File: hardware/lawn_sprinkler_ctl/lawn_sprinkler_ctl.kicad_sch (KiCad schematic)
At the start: 63 parts, among them J1 Terminal_01x14, J2 USB_C_Receptacle_USB2.0_16P, Q1 BT136-600, Q2 BT136-600, Q3 BT136-600, Q4 BT136-600, Q5 BT136-600, Q6 BT136-600, SW1 Reset, SW2 Cde_EV_1, SW3 Cd_EV_2, SW4 Cde_EV_3, SW5 Cde_EV_4, SW6 Cde_EV_5, SW7 Cde_EV_6, U1 mini_esp32, U2 MP1584EN, U3 MOC3041M, U4 MOC3041M, U5 MOC3041M, U6 MOC3041M, U7 MOC3041M, U8 MOC3041M

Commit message: kicad schematic V0.2
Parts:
- removed C2, C3, C4, C5, C6, C7, C8: 10nF, Capacitor_SMD:C_0805_2012Metric, symbol Device:C
- removed D+, Vbus: ~, Connector_JST:JST_PH_S4B-PH-K_1x04_P2.00mm_Horizontal, symbol Mechanical:MountingHole
- removed D-, GND: ~, symbol Mechanical:MountingHole
- removed J2: USB_C_Receptacle_USB2.0_16P, symbol Connector:USB_C_Receptacle_USB2.0_16P
- removed Q2, Q4, Q6: BT136-600, Package_TO_SOT_THT:TO-220F-3_Horizontal_TabDown, symbol Triac_Thyristor:BT136-600
- removed R20: 220, Resistor_SMD:R_0805_2012Metric, symbol Device:R
- added C2: 10uF, Capacitor_THT:CP_Radial_D8.0mm_P3.50mm, symbol Device:C_Polarized
- added D9: LED, symbol Device:LED
- added Q10, Q12: BT136-600, Package_TO_SOT_THT:TO-220-3_Vertical, symbol Triac_Thyristor:BT136-600
- added Q11, Q2, Q4, Q6, Q7, Q9: BC547, Package_TO_SOT_THT:TO-92_Inline, symbol Transistor_BJT:BC547
- added Q8: BT136-600, Package_TO_SOT_SMD:TO-252-3_TabPin2, symbol Triac_Thyristor:BT136-600
- added R21, R22, R24, R25, R26: 330, Resistor_SMD:R_0805_2012Metric, symbol Device:R
- added R23: 10k, symbol Device:R
- added R27: 330, symbol Device:R
- D1: value LED red -> LED
- D8: value LED blue -> LED
- Q1, Q3, Q5: footprint Package_TO_SOT_THT:TO-220F-3_Horizontal_TabDown -> Package_TO_SOT_THT:TO-220-3_Vertical
- R13, R17, R4, R5, R9: value 330 -> 10k; footprint Resistor_SMD:R_0805_2012Metric -> (none)
- U2: value MP1584EN -> FULARR_MP1584EN
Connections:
- net +3.3V: now also C2.1
- net 24VAC_2: now also R15.2, R7.2, Q10.2 (A2), Q12.2 (A2), Q8.2 (A2), R21.2, R25.2; no longer R14.2, R17.2, R5.2, R8.2
- net Cmd_1: now also R4.1; no longer U3.2
- net Cmd_2: now also R5.1; no longer U4.2
- net Cmd_3: now also R9.1; no longer U5.2
- net Cmd_4: now also R13.1; no longer U6.2
- net Cmd_5: now also R17.1; no longer U7.2
- net Cmd_6: now also R23.1; no longer U8.2
- net EV2: now also Q3.1 (A1), R8.2; no longer R6.2
- net EV3: now also Q5.1 (A1), R12.2; no longer Q3.1 (A1), R9.2
- net EV4: now also R16.2, Q8.1 (A1); no longer R12.2
- net EV5: now also Q10.1 (A1), R22.2; no longer Q5.1 (A1), R15.2
- net EV6: now also Q12.1 (A1), R26.2; no longer R18.2
- net GND: now also C2.2, D9.1 (K), Q11.3 (E), Q2.3 (E), Q4.3 (E), Q6.3 (E), Q7.3 (E), Q9.3 (E)
- net at R10.2: now also U5.1; no longer U6.1
- net at R12.1: now also Q5.3 (G), U5.4; no longer U6.4
- net at R11.1: now also U5.6; no longer U6.6
- net at D6.1 (K): now also R18.1; no longer R13.1
- net at U8.6: now also R25.1; no longer R17.1
- net at R8.1: now also Q3.3 (G), U4.4; no longer U5.6
- net at SW1.2: now also U1.2 (RST)
- net at R13.2: now also Q6.2 (B); no longer U7.1
- net at U7.6: now also R21.1; no longer R14.1
- net at D7.1 (K): now also R24.1; no longer R16.1
- net at U4.6: now also R7.1; no longer R5.1
- net at D3.1 (K): now also R6.1; no longer R4.1
- net at U4.1: now also R6.2; no longer R4.2
- net at D4.1 (K): now also R10.1; no longer R7.1
- net at U8.1: now also R24.2; no longer R16.2
- net at U8.4: now also Q12.3 (G), R26.1; no longer R18.1
- net at D5.1 (K): now also R14.1; no longer R10.1
- net at U1.27 (IO_21/D2/SDA): now also R27.1
- new net: D9.2 (A), R27.2
- new net: Q4.1 (C), U5.2
- new net: Q4.2 (B), R9.2
- new net: Q6.1 (C), U6.2
- new net: Q9.2 (B), R17.2
- new net: Q2.2 (B), R5.2
- new net: Q11.1 (C), U8.2
- new net: Q11.2 (B), R23.2
- new net: Q8.3 (G), R16.1, U6.4
- new net: Q7.1 (C), U3.2
- new net: Q7.2 (B), R4.2
- new net: Q2.1 (C), U4.2
- new net: R15.1, U6.6
- new net: R18.2, U7.1
- new net: Q9.1 (C), U7.2
- new net: Q10.3 (G), R22.1, U7.4
- new net: R14.2, U6.1
- no-connect marks 20 -> 26
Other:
- note added: "EVs command"
- note added: "EVs manual control"
- note added: "Microcontroller module"
- note added: "power supply"
- note added: "terminal to EVs, 24VAC"
- moved on the sheet: C1, D1, D2, Q1, R1, R19, R2, R3, SW1, U1, U3

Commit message: feat: update hardware
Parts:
- removed D7: LED, LED_THT:LED_D5.0mm, symbol Device:LED_Small
- removed D8, D9: LED, symbol Device:LED
- removed J1: Terminal_01x14, symbol Connector:Screw_Terminal_01x14
- removed Q11, Q9: BC547, Package_TO_SOT_THT:TO-92_Inline, symbol Transistor_BJT:BC547
- removed Q3, Q5: BT136-600, Package_TO_SOT_THT:TO-220-3_Vertical, symbol Triac_Thyristor:BT136-600
- removed R19: 330, symbol Device:R
- removed SW1: Reset, symbol Switch:SW_Push
- removed U1: mini_esp32, symbol ESP32_mini:mini_esp32
- removed U7, U8: MOC3041M, Package_DIP:DIP-6_W7.62mm, symbol Relay_SolidState:MOC3041M
- added D2, D8, D9: LED, LED_THT:LED_D5.0mm, symbol Device:LED_Small
- added J1, J10, J11, J12, J13, J14, J2, J3, J4, J5, J6, J7, J8, J9: Screw_Terminal_01x01, Carbonaro:square_pad, symbol Connector:Screw_Terminal_01x01
- added J15: Conn_01x04, Connector_PinHeader_2.54mm:PinHeader_1x06_P2.54mm_Vertical, symbol Connector_Generic:Conn_01x06
- added Q11, Q9: BT136-600, Package_TO_SOT_SMD:TO-252-3_TabPin2, symbol Triac_Thyristor:BT136-600
- added Q3, Q5: BC547, Package_TO_SOT_THT:TO-92_Inline, symbol Transistor_BJT:BC547
- added R2, R4: 10k, Resistor_SMD:R_0805_2012Metric_Pad1.20x1.40mm_HandSolder, symbol Device:R
- added R28, R29, R30, R31, R32: 330, Resistor_SMD:R_0805_2012Metric_Pad1.20x1.40mm_HandSolder, symbol Device:R
- added R33, R34: 1k, Resistor_SMD:R_0805_2012Metric_Pad1.20x1.40mm_HandSolder, symbol Device:R_Small
- added SW7: Reset, Button_Switch_THT:SW_PUSH-12mm_Wuerth-430476085716, symbol Switch:SW_Push
- added U2, U3: MOC3041M, Package_DIP:DIP-6_W7.62mm, symbol Relay_SolidState:MOC3041M
- added U8: ESP32-C6-DevKitC-1, Carbonaro:ESP32-C6_DevKit_N8, symbol Espressif:ESP32-C6-DevKitC-1
- C2: footprint Capacitor_THT:CP_Radial_D8.0mm_P3.50mm -> Capacitor_THT:C_Radial_D5.0mm_H11.0mm_P2.00mm
- Q10, Q12: footprint Package_TO_SOT_THT:TO-220-3_Vertical -> Package_TO_SOT_SMD:TO-252-3_TabPin2
- Q7: renamed from Q1; footprint Package_TO_SOT_THT:TO-220-3_Vertical -> Package_TO_SOT_SMD:TO-252-3_TabPin2
- R1: renamed from R4; footprint (none) -> Resistor_SMD:R_0805_2012Metric_Pad1.20x1.40mm_HandSolder
- R10, R11, R12, R21, R22, R24, R25, R26, R7, R8: footprint Resistor_SMD:R_0805_2012Metric -> Resistor_SMD:R_0805_2012Metric_Pad1.20x1.40mm_HandSolder
- R13, R17: value 10k -> 1k; footprint (none) -> Resistor_SMD:R_0805_2012Metric_Pad1.20x1.40mm_HandSolder
- R14, R15, R16, R18: value 330 -> 1k; footprint Resistor_SMD:R_0805_2012Metric -> Resistor_SMD:R_0805_2012Metric_Pad1.20x1.40mm_HandSolder
- R19: renamed from R1; footprint Resistor_SMD:R_0805_2012Metric -> Resistor_SMD:R_0805_2012Metric_Pad1.20x1.40mm_HandSolder
- R20: renamed from R2; footprint Resistor_SMD:R_0805_2012Metric -> Resistor_SMD:R_0805_2012Metric_Pad1.20x1.40mm_HandSolder
- R23, R9: value 10k -> 330; footprint (none) -> Resistor_SMD:R_0805_2012Metric_Pad1.20x1.40mm_HandSolder
- R27, R5: footprint (none) -> Resistor_SMD:R_0805_2012Metric_Pad1.20x1.40mm_HandSolder
- R3, R6: value 330 -> 10k; footprint Resistor_SMD:R_0805_2012Metric -> Resistor_SMD:R_0805_2012Metric_Pad1.20x1.40mm_HandSolder
- SW1: renamed from SW2; footprint (none) -> Button_Switch_THT:SW_PUSH-12mm_Wuerth-430476085716
- SW2: renamed from SW3; value Cd_EV_2 -> Cde_EV_2; footprint (none) -> Button_Switch_THT:SW_PUSH-12mm_Wuerth-430476085716
- SW3: renamed from SW4; footprint (none) -> Button_Switch_THT:SW_PUSH-12mm_Wuerth-430476085716
- SW4: renamed from SW5; footprint (none) -> Button_Switch_THT:SW_PUSH-12mm_Wuerth-430476085716
- SW5: renamed from SW6; footprint (none) -> Button_Switch_THT:SW_PUSH-12mm_Wuerth-430476085716
- SW6: renamed from SW7; footprint (none) -> Button_Switch_THT:SW_PUSH-12mm_Wuerth-430476085716
- U7: renamed from U2; footprint Olivier:FULARR_MP1584EN -> Carbonaro:FULARR_MP1584EN; symbol Olivier:FULARR_MP1584EN -> Carbonaro:FULARR_MP1584EN
- renumbered D2 to D7, Q7 to Q1, U3 to U1
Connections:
- net +3.3V: now also R10.1, R11.1, R12.1, R7.1, R8.1, R9.1, D2.2 (A), J15.1 (Pin_1), R33.1, R34.1, U8.1 (3V3)
- net 24VAC_1: now also J1.1 (Pin_1), J5.1 (Pin_1)
- net 24VAC_2: now also R23.2, R27.2, J2.1 (Pin_1), Q11.2 (A2), Q9.2 (A2), R29.2; no longer R11.2, R15.2, R7.2
- net Cmd_1: now also U8.23 (GPIO18)
- net Cmd_2: now also R2.1, U8.24 (GPIO19); no longer R5.1
- net Cmd_3: now also R3.1, U8.25 (GPIO20); no longer R9.1
- net Cmd_4: now also R4.1, U8.26 (GPIO21); no longer R13.1
- net Cmd_5: now also R5.1, U8.27 (GPIO22); no longer R17.1
- net Cmd_6: now also R6.1, U8.28 (GPIO23); no longer R23.1
- net EV1: now also J7.1 (Pin_1)
- net EV2: now also Q8.1 (A1), R22.2, J8.1 (Pin_1); no longer R8.2
- net EV3: now also R24.2, J9.1 (Pin_1), Q9.1 (A1); no longer R12.2
- net EV4: now also Q10.1 (A1), R26.2, J10.1 (Pin_1); no longer Q8.1 (A1), R16.2
- net EV5: now also J11.1 (Pin_1), Q11.1 (A1), R28.2; no longer Q10.1 (A1), R22.2
- net EV6: now also J12.1 (Pin_1), R30.2; no longer R26.2
- net GND: now also C1.2, D7.2 (-), U7.2 (IN-), D8.1 (K), D9.1 (K), J15.6 (Pin_6), Q3.3 (E), Q5.3 (E), SW7.1, U8.15 (GND), U8.18 (GND), U8.21 (GND), U8.32 (GND)
- net SW_1: now also U8.3 (GPIO4/MTMS)
- net SW_2: now also U8.4 (GPIO5/MTDI)
- net SW_3: now also U8.5 (GPIO6)
- net SW_4: now also U8.6 (GPIO7)
- net SW_5: now also U8.9 (GPIO8/BOOT)
- net SW_6: now also U8.22 (GPIO9/BOOT)
- net at U5.6: now also R27.1; no longer R11.1
- net at Q4.1 (C): now also U4.2; no longer U5.2
- net at Q4.2 (B): now also R4.2; no longer R9.2
- net at Q6.2 (B): now also R6.2; no longer R13.2
- net at R24.1: now also Q9.3 (G), U3.4
- net at D3.1 (K): now also R15.1; no longer R6.1
- net at U4.1: now also R10.2, R16.2; no longer R6.2
- net at U5.4: now also Q11.3 (G), R28.1; no longer R12.1
- net at R17.2: now also R11.2, U5.1
- net at U4.4: now also Q10.3 (G), R26.1; no longer R8.1
- net at Q2.2 (B): now also R2.2; no longer R5.2
- net at D1.1 (K): now also R13.1; no longer R3.1
- net at U1.1: now also R13.2, R7.2; no longer R3.2
- net at D4.1 (K): now also R16.1; no longer R10.1
- net at Q2.1 (C): now also U2.2; no longer U4.2
- net at Q12.3 (G): now also U6.4, R30.1; no longer R26.1
- net at R25.1: now also U4.6
- net at U6.6: now also R29.1; no longer R15.1
- net at R18.2: now also R12.2, U6.1
- net at R22.1: now also Q8.3 (G), U2.4; no longer Q10.3 (G)
- net at R21.1: now also U2.6
- net at R14.1: now also D2.1 (K); no longer D5.1 (K)
- net at R14.2: now also R8.2, U2.1; no longer U6.1
- new net: R15.2, R9.2, U3.1
- new net: Q3.1 (C), U3.2
- new net: R23.1, U3.6
- new net: Q3.2 (B), R3.2
- new net: Q5.1 (C), U5.2
- new net: Q5.2 (B), R5.2
- new net: D8.2 (A), R31.1
- new net: R31.2, U8.10 (GPIO10)
- new net: D9.2 (A), R32.1
- new net: R32.2, U8.11 (GPIO11)
- new net: D5.1 (K), R17.1
- new net: SW7.2, U8.2 (EN/RESET)
- new net GPIO0: J15.5 (Pin_5), U8.7 (GPIO0)
- new net GPIO1: J15.4 (Pin_4), U8.8 (GPIO1)
- new net GPIO2: J15.3 (Pin_3), R33.2, U8.12 (GPIO2)
- new net GPIO3: J15.2 (Pin_2), R34.2, U8.13 (GPIO3)
- no-connect marks 26 -> 11
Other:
- note added: "Power Supply"
- note added: "Test points"
- note removed: "power supply"
- moved on the sheet: C1, C2, D1, D7, Q1, Q7, R1, R19, R20, U1, U7

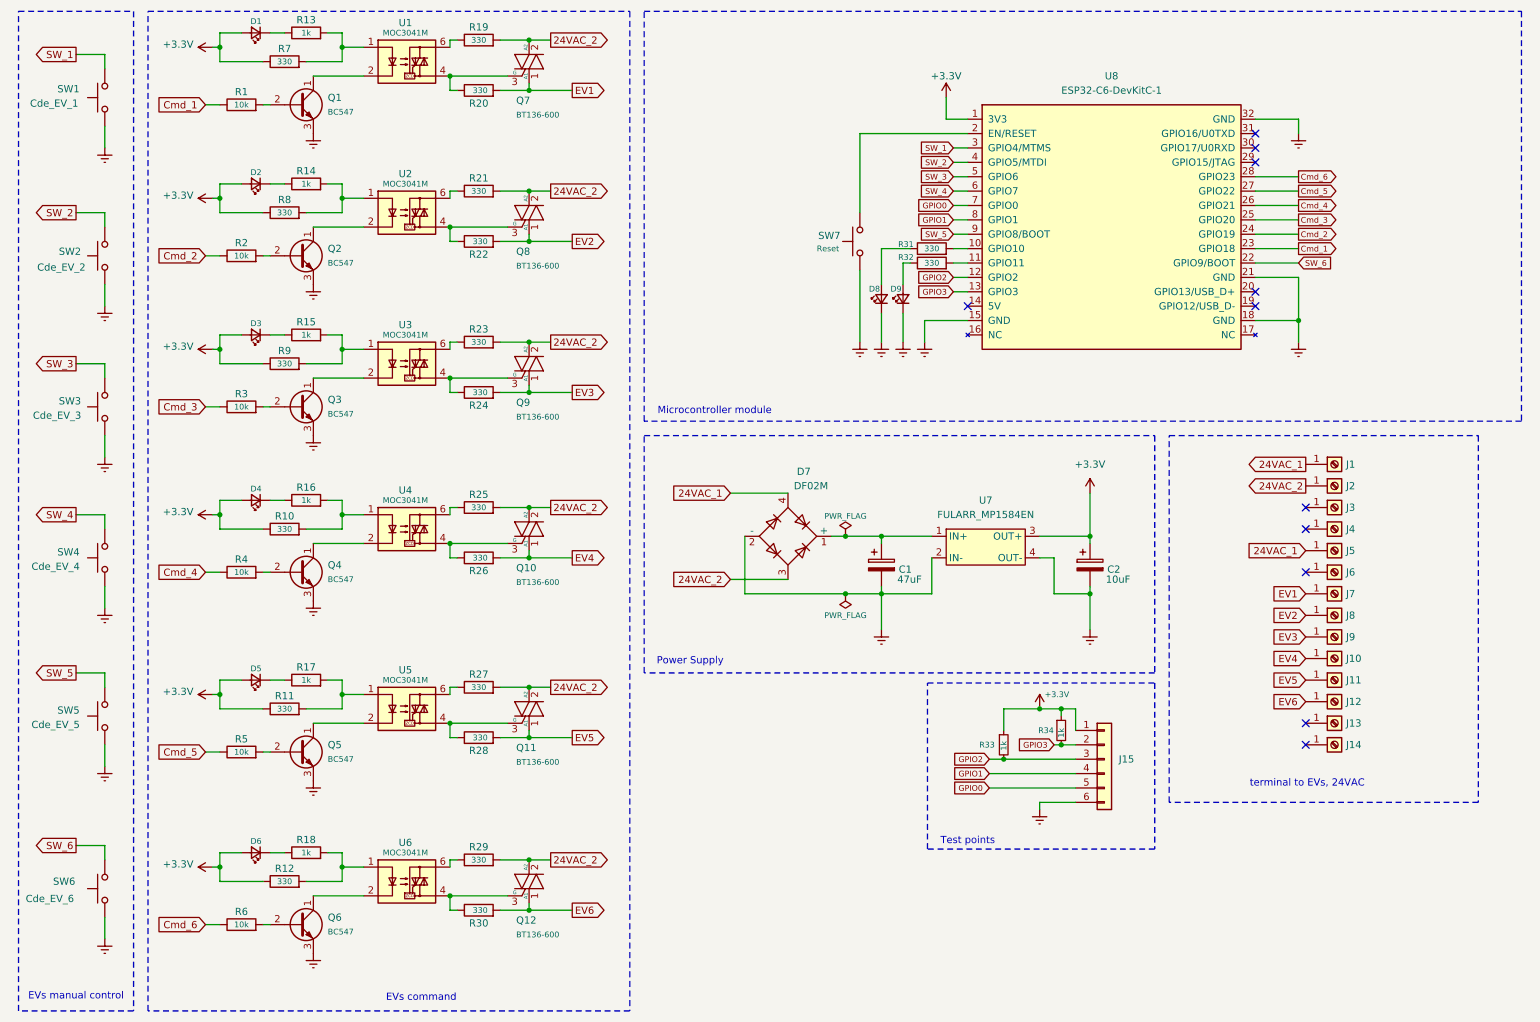
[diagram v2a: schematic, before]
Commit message: feat: update schematics resistors
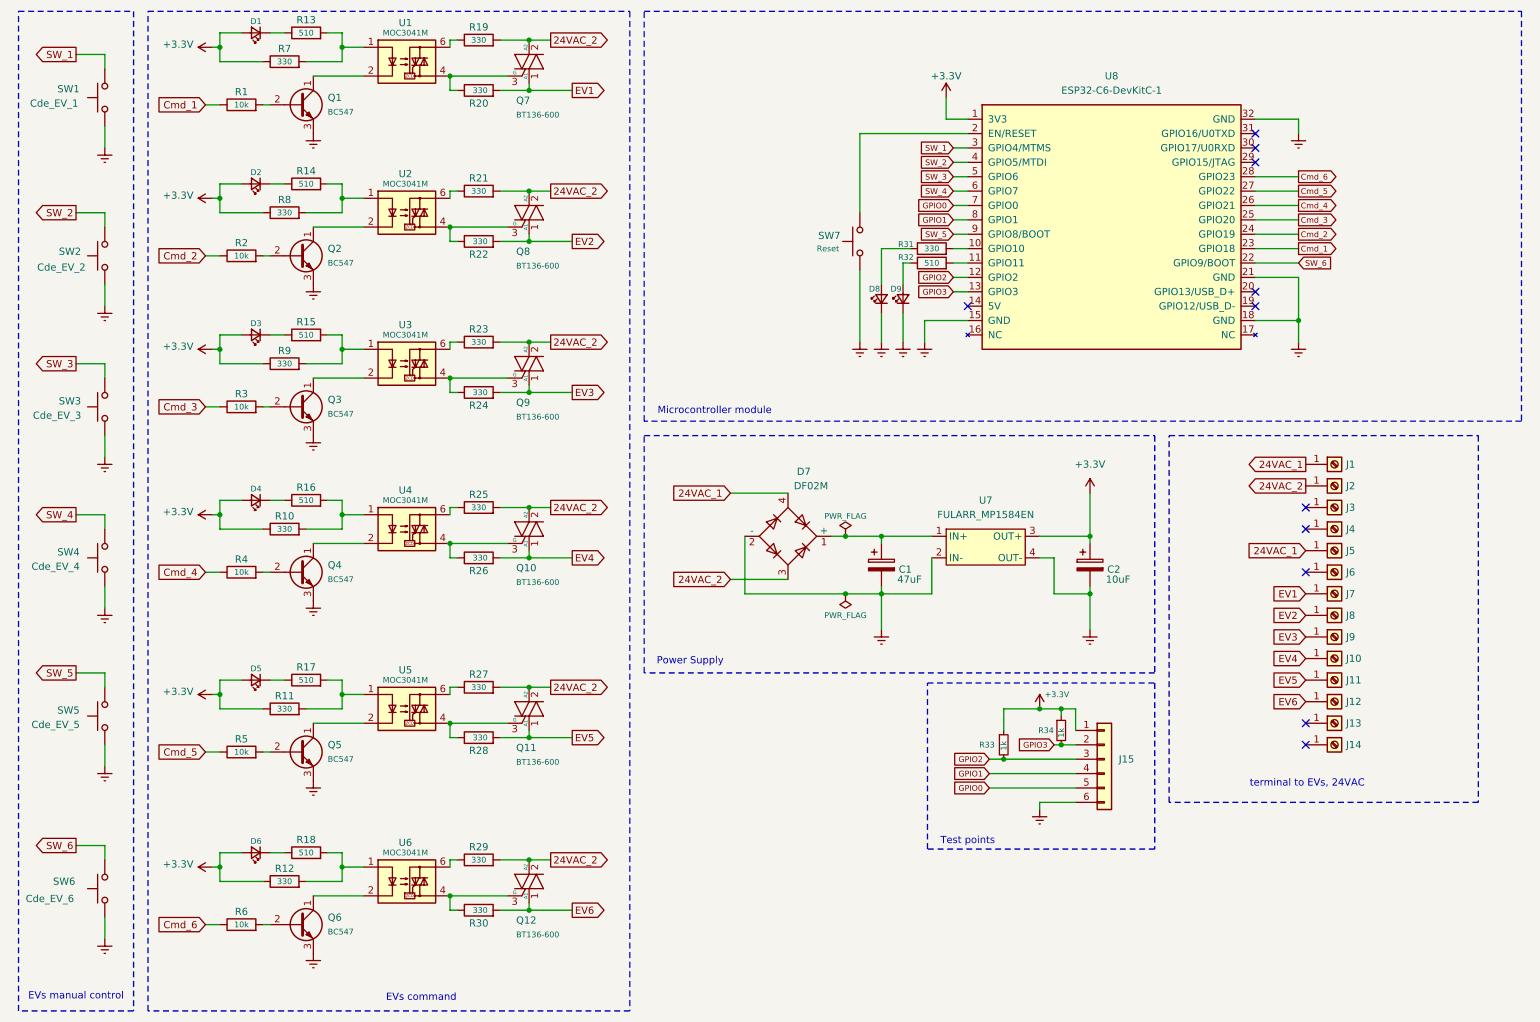
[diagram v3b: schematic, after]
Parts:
- R13, R14, R15, R16, R17, R18: value 1k -> 510
- R32: value 330 -> 510
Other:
- company: (none) -> O & A.Carbonaro
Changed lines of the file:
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@@
 	(title_block
 		(title "Lawn Sprinkler Controller")
-		(date "2026-05-15")
-		(rev "1.1")
+		(date "2026-06-15")
+		(rev "1.2")
+		(company "O & A.Carbonaro")
 		(comment 1 "1.0 : final version for production")
 		(comment 2 "1.1 : R33 & R34 value set to 1k")
+		(comment 3 "1.2 : R13 to R18 set to 510 Ohm, R32 set to 510 Ohm")
 	)
 	(rectangle
@@
 			)
 		)
-		(property "Value" "1k"
+		(property "Value" "510"
 			(at 67.31 20.32 90)
 			(effects
@@
 			)
 		)
-		(property "Value" "1k"
+		(property "Value" "510"
 			(at 67.31 165.1 90)
 			(effects
@@
 			)
 		)
-		(property "Value" "330"
+		(property "Value" "510"
 			(at 177.8 60.96 90)
 			(effects
@@
 			)
 		)
-		(property "Value" "1k"
+		(property "Value" "510"
 			(at 67.31 46.99 90)
 			(effects
@@
 			)
 		)
-		(property "Value" "1k"
+		(property "Value" "510"
 			(at 67.31 134.62 90)
 			(effects
@@
 			)
 		)
-		(property "Value" "1k"
+		(property "Value" "510"
 			(at 67.31 102.87 90)
 			(effects
@@
 			)
 		)
-		(property "Value" "1k"
+		(property "Value" "510"
 			(at 67.31 73.66 90)
 			(effects
